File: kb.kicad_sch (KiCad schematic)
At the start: 190 parts, among them J1 Conn_02x04, J2 10029449-001RLF, J3 Conn_01x05, J4 Conn_01x10, J5 Conn_01x07, J6 Conn_01x06, SW1 RotaryEncoder_Switch, U1 Pico, U2 TXB0101DBVR

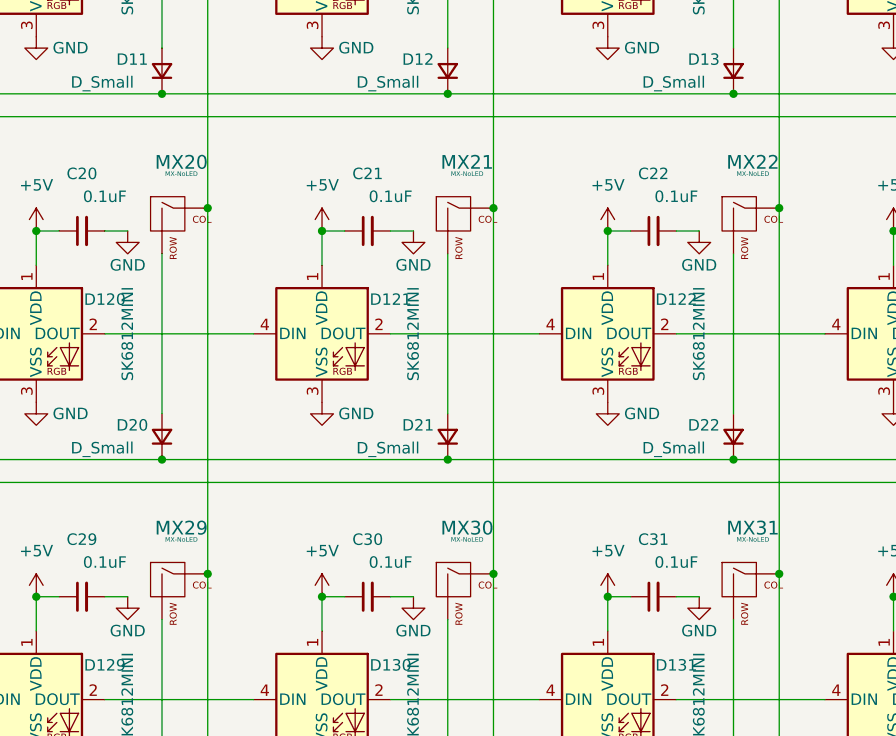
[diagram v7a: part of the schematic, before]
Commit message: added stepped capslock support
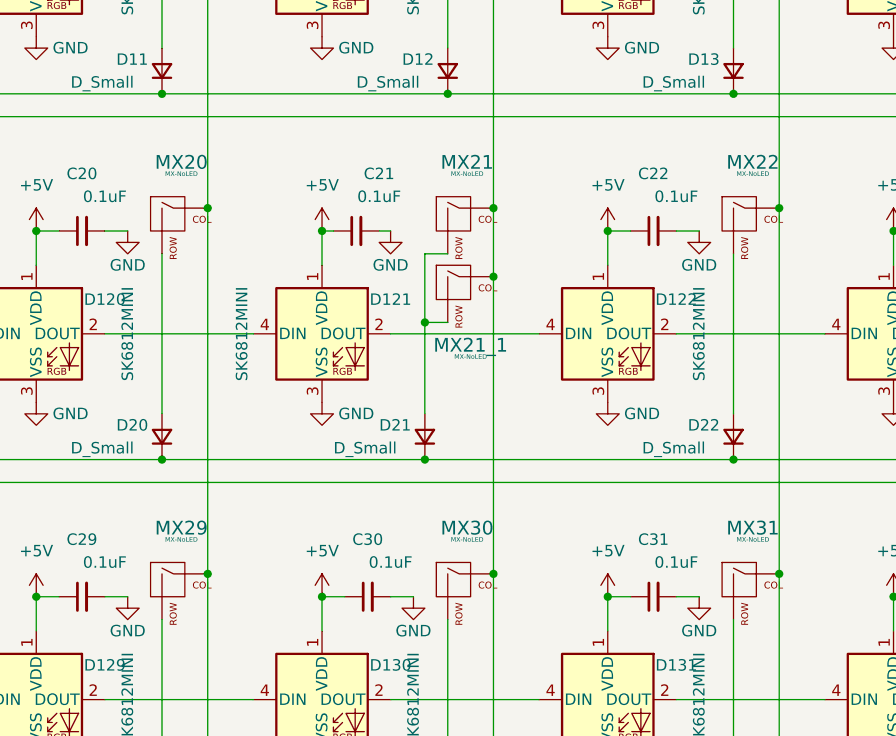
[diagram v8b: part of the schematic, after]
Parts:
- added MX21_1: MX-NoLED, MX_Only:MXOnly-1.25U-Hotswap, symbol MX_Alps_Hybrid:MX-NoLED
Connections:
- net COL3: now also MX21_1.1 (COL)
- net at D21.2 (A), MX21.2 (ROW): now also MX21_1.2 (ROW)
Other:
- moved on the sheet: C21, D21
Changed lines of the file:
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@@
   (junction (at 342.9 142.24) (diameter 0) (color 0 0 0 0)
   )
+  (junction (at 144.78 173.99) (diameter 0) (color 0 0 0 0)
+  )
   (junction (at 274.32 107.95) (diameter 0) (color 0 0 0 0)
   )
@@
   (junction (at 115.57 148.59) (diameter 0) (color 0 0 0 0)
   )
+  (junction (at 152.4 168.91) (diameter 0) (color 0 0 0 0)
+  )
   (junction (at 179.07 270.51) (diameter 0) (color 0 0 0 0)
   )
@@
   (junction (at 69.85 123.19) (diameter 0) (color 0 0 0 0)
   )
-  (junction (at 147.32 189.23) (diameter 0) (color 0 0 0 0)
-  )
   (junction (at 133.35 163.83) (diameter 0) (color 0 0 0 0)
   )
@@
   (junction (at 274.32 148.59) (diameter 0) (color 0 0 0 0)
   )
+  (junction (at 144.78 189.23) (diameter 0) (color 0 0 0 0)
+  )
   (junction (at 101.6 204.47) (diameter 0) (color 0 0 0 0)
   )
@@
     (stroke (width 0) (type default) (color 0 0 0 0))
   )
-  (wire (pts (xy 133.35 163.83) (xy 135.89 163.83))
+  (wire (pts (xy 133.35 163.83) (xy 134.62 163.83))
     (stroke (width 0) (type default) (color 0 0 0 0))
   )
@@
     (stroke (width 0) (type default) (color 0 0 0 0))
   )
+  (wire (pts (xy 144.78 166.37) (xy 147.32 166.37))
+    (stroke (width 0) (type default) (color 0 0 0 0))
+  )
   (wire (pts (xy 196.85 245.11) (xy 199.39 245.11))
     (stroke (width 0) (type default) (color 0 0 0 0))
@@
     (stroke (width 0) (type default) (color 0 0 0 0))
   )
-  (wire (pts (xy 152.4 161.29) (xy 152.4 201.93))
+  (wire (pts (xy 152.4 161.29) (xy 152.4 168.91))
     (stroke (width 0) (type default) (color 0 0 0 0))
   )
@@
     (stroke (width 0) (type default) (color 0 0 0 0))
   )
+  (wire (pts (xy 144.78 173.99) (xy 147.32 173.99))
+    (stroke (width 0) (type default) (color 0 0 0 0))
+  )
   (wire (pts (xy 165.1 163.83) (xy 165.1 167.64))
     (stroke (width 0) (type default) (color 0 0 0 0))
@@
     (stroke (width 0) (type default) (color 0 0 0 0))
   )
-  (wire (pts (xy 115.57 189.23) (xy 147.32 189.23))
+  (wire (pts (xy 115.57 189.23) (xy 144.78 189.23))
     (stroke (width 0) (type default) (color 0 0 0 0))
   )
@@
     (stroke (width 0) (type default) (color 0 0 0 0))
   )
-  (wire (pts (xy 147.32 166.37) (xy 147.32 184.15))
+  (wire (pts (xy 144.78 166.37) (xy 144.78 173.99))
     (stroke (width 0) (type default) (color 0 0 0 0))
   )
@@
     (stroke (width 0) (type default) (color 0 0 0 0))
   )
+  (wire (pts (xy 152.4 168.91) (xy 152.4 201.93))
+    (stroke (width 0) (type default) (color 0 0 0 0))
+  )
   (wire (pts (xy 236.22 215.9) (xy 252.73 215.9))
     (stroke (width 0) (type default) (color 0 0 0 0))
@@
     (stroke (width 0) (type default) (color 0 0 0 0))
   )
-  (wire (pts (xy 140.97 163.83) (xy 143.51 163.83))
+  (wire (pts (xy 139.7 163.83) (xy 140.97 163.83))
     (stroke (width 0) (type default) (color 0 0 0 0))
   )
@@
     (stroke (width 0) (type default) (color 0 0 0 0))
   )
-  (wire (pts (xy 147.32 189.23) (xy 179.07 189.23))
+  (wire (pts (xy 144.78 189.23) (xy 179.07 189.23))
     (stroke (width 0) (type default) (color 0 0 0 0))
   )
@@
     (stroke (width 0) (type default) (color 0 0 0 0))
   )
+  (wire (pts (xy 144.78 173.99) (xy 144.78 184.15))
+    (stroke (width 0) (type default) (color 0 0 0 0))
+  )
   (label "RGB_5V" (at 41.91 40.64 180)
     (effects (font (size 1.27 1.27)) (justify right bottom))
@@
     (pin "4")
   )
+  (symbol (lib_id "MX_Alps_Hybrid:MX-NoLED") (at 148.59 170.18 0) (unit 1)
+    (in_bom yes) (on_board yes)
+    (property "Reference" "MX21_1" (id 0) (at 149.86 176.53 0)
+      (effects (font (size 1.524 1.524)))
+    )
+    (property "Value" "MX-NoLED" (id 1) (at 149.86 177.8 0)
+      (effects (font (size 0.508 0.508)))
+    )
+    (property "Footprint" "MX_Only:MXOnly-1.25U-Hotswap" (id 2) (at 132.715 170.815 0)
+      (effects (font (size 1.524 1.524)) hide)
+    )
+    (property "Datasheet" "" (id 3) (at 132.715 170.815 0)
+      (effects (font (size 1.524 1.524)) hide)
+    )
+    (pin "1")
+    (pin "2")
+  )
   (symbol (lib_id "LED:WS2812B") (at 69.85 93.98 0) (unit 1)
     (in_bom yes) (on_board yes)
@@
     (in_bom yes) (on_board yes)
     (property "Reference" "D121" (id 0) (at 140.97 171.45 0))
-    (property "Value" "SK6812MINI" (id 1) (at 143.51 175.26 90))
+    (property "Value" "SK6812MINI" (id 1) (at 124.46 175.26 90))
     (property "Footprint" "Keebio-Parts:SK6812-MINI-E" (id 2) (at 134.62 182.88 0)
       (effects (font (size 1.27 1.27)) (justify left top) hide)
@@
     (pin "1")
   )
-  (symbol (lib_id "power:GND") (at 143.51 163.83 0) (unit 1)
+  (symbol (lib_id "power:GND") (at 140.97 163.83 0) (unit 1)
     (in_bom yes) (on_board yes)
-    (property "Reference" "#PWR073" (id 0) (at 143.51 170.18 0)
+    (property "Reference" "#PWR073" (id 0) (at 140.97 170.18 0)
       (effects (font (size 1.27 1.27)) hide)
     )
-    (property "Value" "GND" (id 1) (at 143.51 167.64 0))
-    (property "Footprint" "" (id 2) (at 143.51 163.83 0)
+    (property "Value" "GND" (id 1) (at 140.97 167.64 0))
+    (property "Footprint" "" (id 2) (at 140.97 163.83 0)
       (effects (font (size 1.27 1.27)) hide)
     )
-    (property "Datasheet" "" (id 3) (at 143.51 163.83 0)
+    (property "Datasheet" "" (id 3) (at 140.97 163.83 0)
       (effects (font (size 1.27 1.27)) hide)
     )
@@
     (pin "2")
   )
-  (symbol (lib_id "Device:D_Small") (at 147.32 186.69 90) (unit 1)
+  (symbol (lib_id "Device:D_Small") (at 144.78 186.69 90) (unit 1)
     (in_bom yes) (on_board yes)
-    (property "Reference" "D21" (id 0) (at 142.24 185.42 90)
+    (property "Reference" "D21" (id 0) (at 139.7 185.42 90)
       (effects (font (size 1.27 1.27)) (justify right))
     )
-    (property "Value" "D_Small" (id 1) (at 137.16 187.96 90)
+    (property "Value" "D_Small" (id 1) (at 134.62 187.96 90)
       (effects (font (size 1.27 1.27)) (justify right))
     )
-    (property "Footprint" "Diode_SMD:D_SOD-123" (id 2) (at 147.32 186.69 90)
+    (property "Footprint" "Diode_SMD:D_SOD-123" (id 2) (at 144.78 186.69 90)
       (effects (font (size 1.27 1.27)) hide)
     )
-    (property "Datasheet" "~" (id 3) (at 147.32 186.69 90)
+    (property "Datasheet" "~" (id 3) (at 144.78 186.69 90)
       (effects (font (size 1.27 1.27)) hide)
     )
@@
   )
   (symbol (lib_id "MX_Alps_Hybrid:MX-NoLED") (at 148.59 162.56 0) (unit 1)
-    (in_bom yes) (on_board yes) (fields_autoplaced)
+    (in_bom yes) (on_board yes)
     (property "Reference" "MX21" (id 0) (at 149.4756 156.21 0)
       (effects (font (size 1.524 1.524)))
@@
     (pin "1")
   )
-  (symbol (lib_id "Device:C_Small") (at 138.43 163.83 90) (unit 1)
+  (symbol (lib_id "Device:C_Small") (at 137.16 163.83 90) (unit 1)
     (in_bom yes) (on_board yes)
-    (property "Reference" "C21" (id 0) (at 138.43 157.48 90))
-    (property "Value" "0.1uF" (id 1) (at 140.97 160.02 90))
-    (property "Footprint" "Capacitor_SMD:C_0805_2012Metric_Pad1.18x1.45mm_HandSolder" (id 2) (at 138.43 163.83 0)
+    (property "Reference" "C21" (id 0) (at 139.7 157.48 90))
+    (property "Value" "0.1uF" (id 1) (at 139.7 160.02 90))
+    (property "Footprint" "Capacitor_SMD:C_0805_2012Metric_Pad1.18x1.45mm_HandSolder" (id 2) (at 137.16 163.83 0)
       (effects (font (size 1.27 1.27)) hide)
     )
-    (property "Datasheet" "~" (id 3) (at 138.43 163.83 0)
+    (property "Datasheet" "~" (id 3) (at 137.16 163.83 0)
       (effects (font (size 1.27 1.27)) hide)
     )
@@
       (reference "MX21") (unit 1) (value "MX-NoLED") (footprint "MX_Only:MXOnly-1.75U-Hotswap")
     )
+    (path "/13335042-2697-4e6d-9055-f641b7432626"
+      (reference "MX21_1") (unit 1) (value "MX-NoLED") (footprint "MX_Only:MXOnly-1.25U-Hotswap")
+    )
     (path "/f2a56274-1dcc-40cf-be33-d18b36eb2565"
